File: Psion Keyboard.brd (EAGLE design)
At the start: 100 x 80 mm, 3 parts, among them X2 52745-2290

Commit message: Basic board shape.
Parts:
- moved MS1 5.08 mm to (88.9, 22.9)
- moved S2 2.84 mm to (30.5, 19.1)
- moved X2 1.80 mm to (14.0, 16.5)
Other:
- board size 100 x 80 mm -> 88.9 x 22.9 mm
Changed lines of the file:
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@@
 <setting verticaltext="up"/>
 </settings>
-<grid distance="50" unitdist="mil" unit="mil" style="lines" multiple="1" display="yes" altdistance="5" altunitdist="mil" altunit="mil"/>
+<grid distance="50" unitdist="mil" unit="mil" style="lines" multiple="1" display="yes" altdistance="0.1" altunitdist="mil" altunit="mil"/>
 <layers>
 <layer number="1" name="Top" color="4" fill="1" visible="yes" active="yes"/>
@@
 <board>
 <plain>
-<wire x1="0" y1="0" x2="100" y2="0" width="0" layer="20"/>
-<wire x1="100" y1="0" x2="100" y2="80" width="0" layer="20"/>
-<wire x1="100" y1="80" x2="0" y2="80" width="0" layer="20"/>
-<wire x1="0" y1="80" x2="0" y2="0" width="0" layer="20"/>
+<wire x1="0" y1="0" x2="88.9002" y2="0" width="0" layer="20"/>
+<wire x1="88.9002" y1="0" x2="88.900196875" y2="22.860159375" width="0" layer="20"/>
+<wire x1="88.900196875" y1="22.860159375" x2="0" y2="22.860159375" width="0" layer="20"/>
+<wire x1="0" y1="22.860159375" x2="0" y2="0" width="0" layer="20"/>
 <circle x="2.54" y="2.54" radius="1.27" width="0.000025" layer="20"/>
-<circle x="2.54" y="19.05" radius="1.27" width="0.000025" layer="20"/>
+<circle x="2.54" y="20.32" radius="1.27" width="0.000025" layer="20"/>
 </plain>
 <attributes>
@@
 </autorouter>
 <elements>
-<element name="MS1" library="adafruit" library_urn="urn:adsk.eagle:library:420" package="FEATHERWING_DIM" value="FEATHERWING_NODIM" x="93.98" y="22.86" rot="R180"/>
-<element name="S2" library="adafruit" library_urn="urn:adsk.eagle:library:420" package="EG1213" value="EG1213" x="33.02" y="20.32" rot="R180"/>
-<element name="X2" library="con-molex" library_urn="urn:adsk.eagle:library:165" package="52745-2290" value="52745-2290" x="15.24" y="17.78">
-<attribute name="MF" value="MOLEX" x="15.24" y="17.78" size="1.778" layer="27" display="off"/>
-<attribute name="MPN" value="" x="15.24" y="17.78" size="1.778" layer="27" display="off"/>
-<attribute name="OC_FARNELL" value="unknown" x="15.24" y="17.78" size="1.778" layer="27" display="off"/>
-<attribute name="OC_NEWARK" value="unknown" x="15.24" y="17.78" size="1.778" layer="27" display="off"/>
+<element name="MS1" library="adafruit" library_urn="urn:adsk.eagle:library:420" package="FEATHERWING_DIM" value="FEATHERWING_NODIM" x="88.9" y="22.86" rot="R180"/>
+<element name="S2" library="adafruit" library_urn="urn:adsk.eagle:library:420" package="EG1213" value="EG1213" x="30.48" y="19.05" rot="R180"/>
+<element name="X2" library="con-molex" library_urn="urn:adsk.eagle:library:165" package="52745-2290" value="52745-2290" x="13.97" y="16.51">
+<attribute name="MF" value="MOLEX" x="13.97" y="16.51" size="1.778" layer="27" display="off"/>
+<attribute name="MPN" value="" x="13.97" y="16.51" size="1.778" layer="27" display="off"/>
+<attribute name="OC_FARNELL" value="unknown" x="13.97" y="16.51" size="1.778" layer="27" display="off"/>
+<attribute name="OC_NEWARK" value="unknown" x="13.97" y="16.51" size="1.778" layer="27" display="off"/>
 </element>
 </elements>
@@
 <contactref element="S2" pad="1"/>
 <contactref element="MS1" pad="4"/>
-<wire x1="35.02" y1="20.32" x2="80.01" y2="21.59" width="0" layer="19" extent="1-1"/>
+<wire x1="32.48" y1="19.05" x2="74.93" y2="21.59" width="0" layer="19" extent="1-1"/>
 </signal>
 <signal name="EN">
 <contactref element="S2" pad="2"/>
 <contactref element="MS1" pad="27"/>
-<wire x1="33.02" y1="20.32" x2="74.93" y2="1.27" width="0" layer="19" extent="1-1"/>
+<wire x1="30.48" y1="19.05" x2="69.85" y2="1.27" width="0" layer="19" extent="1-1"/>
 </signal>
 <signal name="SDA">
@@
 <contactref element="X2" pad="2"/>
 <contactref element="X2" pad="5"/>
-<wire x1="11.99" y1="20.28" x2="10.49" y2="20.28" width="0" layer="19" extent="1-1"/>
-<wire x1="49.53" y1="1.27" x2="11.99" y2="20.28" width="0" layer="19" extent="1-1"/>
+<wire x1="10.72" y1="19.01" x2="9.22" y2="19.01" width="0" layer="19" extent="1-1"/>
+<wire x1="44.45" y1="1.27" x2="10.72" y2="19.01" width="0" layer="19" extent="1-1"/>
 </signal>
 <signal name="SCL">
 <contactref element="MS1" pad="18"/>
 <contactref element="X2" pad="3"/>
-<wire x1="52.07" y1="1.27" x2="10.99" y2="20.28" width="0" layer="19" extent="1-1"/>
+<wire x1="46.99" y1="1.27" x2="9.72" y2="19.01" width="0" layer="19" extent="1-1"/>
 </signal>
 <signal name="27">
 <contactref element="MS1" pad="19"/>
 <contactref element="X2" pad="4"/>
-<wire x1="54.61" y1="1.27" x2="11.49" y2="20.28" width="0" layer="19" extent="1-1"/>
+<wire x1="49.53" y1="1.27" x2="10.22" y2="19.01" width="0" layer="19" extent="1-1"/>
 </signal>
 <signal name="30">
 <contactref element="MS1" pad="20"/>
 <contactref element="X2" pad="6"/>
-<wire x1="57.15" y1="1.27" x2="12.49" y2="20.28" width="0" layer="19" extent="1-1"/>
+<wire x1="52.07" y1="1.27" x2="11.22" y2="19.01" width="0" layer="19" extent="1-1"/>
 </signal>
 <signal name="11">
 <contactref element="MS1" pad="22"/>
 <contactref element="X2" pad="7"/>
-<wire x1="12.99" y1="20.28" x2="62.23" y2="1.27" width="0" layer="19" extent="1-1"/>
+<wire x1="11.72" y1="19.01" x2="57.15" y2="1.27" width="0" layer="19" extent="1-1"/>
 </signal>
 <signal name="7">
 <contactref element="MS1" pad="23"/>
 <contactref element="X2" pad="8"/>
-<wire x1="13.49" y1="20.28" x2="64.77" y2="1.27" width="0" layer="19" extent="1-1"/>
+<wire x1="12.22" y1="19.01" x2="59.69" y2="1.27" width="0" layer="19" extent="1-1"/>
 </signal>
 <signal name="15">
 <contactref element="MS1" pad="24"/>
 <contactref element="X2" pad="9"/>
-<wire x1="13.99" y1="20.28" x2="67.31" y2="1.27" width="0" layer="19" extent="1-1"/>
+<wire x1="12.72" y1="19.01" x2="62.23" y2="1.27" width="0" layer="19" extent="1-1"/>
 </signal>
 <signal name="16">
 <contactref element="MS1" pad="25"/>
 <contactref element="X2" pad="10"/>
-<wire x1="14.49" y1="20.28" x2="69.85" y2="1.27" width="0" layer="19" extent="1-1"/>
+<wire x1="13.22" y1="19.01" x2="64.77" y2="1.27" width="0" layer="19" extent="1-1"/>
 </signal>
 <signal name="USB">
@@
 <contactref element="MS1" pad="15"/>
 <contactref element="X2" pad="21"/>
-<wire x1="19.99" y1="20.28" x2="52.07" y2="21.59" width="0" layer="19" extent="1-1"/>
+<wire x1="18.72" y1="19.01" x2="46.99" y2="21.59" width="0" layer="19" extent="1-1"/>
 </signal>
 <signal name="RXD">
 <contactref element="MS1" pad="14"/>
 <contactref element="X2" pad="20"/>
-<wire x1="19.49" y1="20.28" x2="54.61" y2="21.59" width="0" layer="19" extent="1-1"/>
+<wire x1="18.22" y1="19.01" x2="49.53" y2="21.59" width="0" layer="19" extent="1-1"/>
 </signal>
 <signal name="MISO">
 <contactref element="MS1" pad="13"/>
 <contactref element="X2" pad="19"/>
-<wire x1="18.99" y1="20.28" x2="57.15" y2="21.59" width="0" layer="19" extent="1-1"/>
+<wire x1="17.72" y1="19.01" x2="52.07" y2="21.59" width="0" layer="19" extent="1-1"/>
 </signal>
 <signal name="MOSI">
 <contactref element="MS1" pad="12"/>
 <contactref element="X2" pad="18"/>
-<wire x1="18.49" y1="20.28" x2="59.69" y2="21.59" width="0" layer="19" extent="1-1"/>
+<wire x1="17.22" y1="19.01" x2="54.61" y2="21.59" width="0" layer="19" extent="1-1"/>
 </signal>
 <signal name="SCK">
 <contactref element="MS1" pad="11"/>
 <contactref element="X2" pad="17"/>
-<wire x1="17.99" y1="20.28" x2="62.23" y2="21.59" width="0" layer="19" extent="1-1"/>
+<wire x1="16.72" y1="19.01" x2="57.15" y2="21.59" width="0" layer="19" extent="1-1"/>
 </signal>
 <signal name="A5">
 <contactref element="MS1" pad="10"/>
 <contactref element="X2" pad="16"/>
-<wire x1="17.49" y1="20.28" x2="64.77" y2="21.59" width="0" layer="19" extent="1-1"/>
+<wire x1="16.22" y1="19.01" x2="59.69" y2="21.59" width="0" layer="19" extent="1-1"/>
 </signal>
 <signal name="A4">
 <contactref element="MS1" pad="9"/>
 <contactref element="X2" pad="15"/>
-<wire x1="16.99" y1="20.28" x2="67.31" y2="21.59" width="0" layer="19" extent="1-1"/>
+<wire x1="15.72" y1="19.01" x2="62.23" y2="21.59" width="0" layer="19" extent="1-1"/>
 </signal>
 <signal name="A3">
 <contactref element="MS1" pad="8"/>
 <contactref element="X2" pad="14"/>
-<wire x1="16.49" y1="20.28" x2="69.85" y2="21.59" width="0" layer="19" extent="1-1"/>
+<wire x1="15.22" y1="19.01" x2="64.77" y2="21.59" width="0" layer="19" extent="1-1"/>
 </signal>
 <signal name="A2">
 <contactref element="MS1" pad="7"/>
 <contactref element="X2" pad="13"/>
-<wire x1="15.99" y1="20.28" x2="72.39" y2="21.59" width="0" layer="19" extent="1-1"/>
+<wire x1="14.72" y1="19.01" x2="67.31" y2="21.59" width="0" layer="19" extent="1-1"/>
 </signal>
 <signal name="A1">
 <contactref element="MS1" pad="6"/>
 <contactref element="X2" pad="12"/>
-<wire x1="15.49" y1="20.28" x2="74.93" y2="21.59" width="0" layer="19" extent="1-1"/>
+<wire x1="14.22" y1="19.01" x2="69.85" y2="21.59" width="0" layer="19" extent="1-1"/>
 </signal>
 <signal name="A0">
 <contactref element="MS1" pad="5"/>
 <contactref element="X2" pad="11"/>
-<wire x1="14.99" y1="20.28" x2="77.47" y2="21.59" width="0" layer="19" extent="1-1"/>
+<wire x1="13.72" y1="19.01" x2="72.39" y2="21.59" width="0" layer="19" extent="1-1"/>
 </signal>
 </signals>

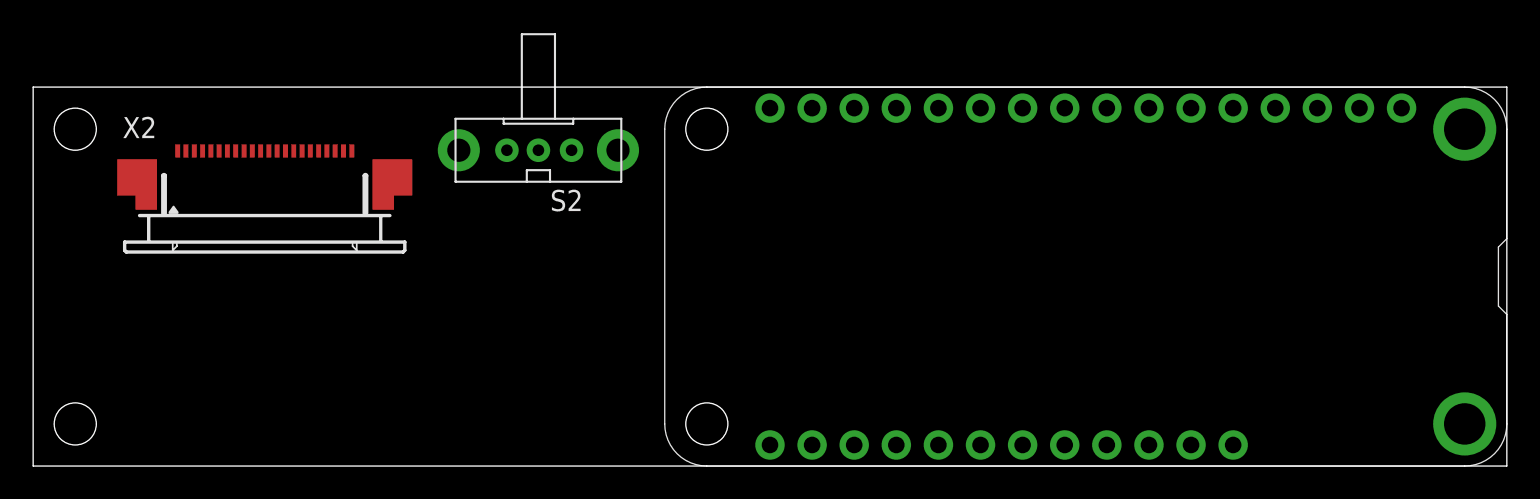
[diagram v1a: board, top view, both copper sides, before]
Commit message: Ignore .job files. General shape.
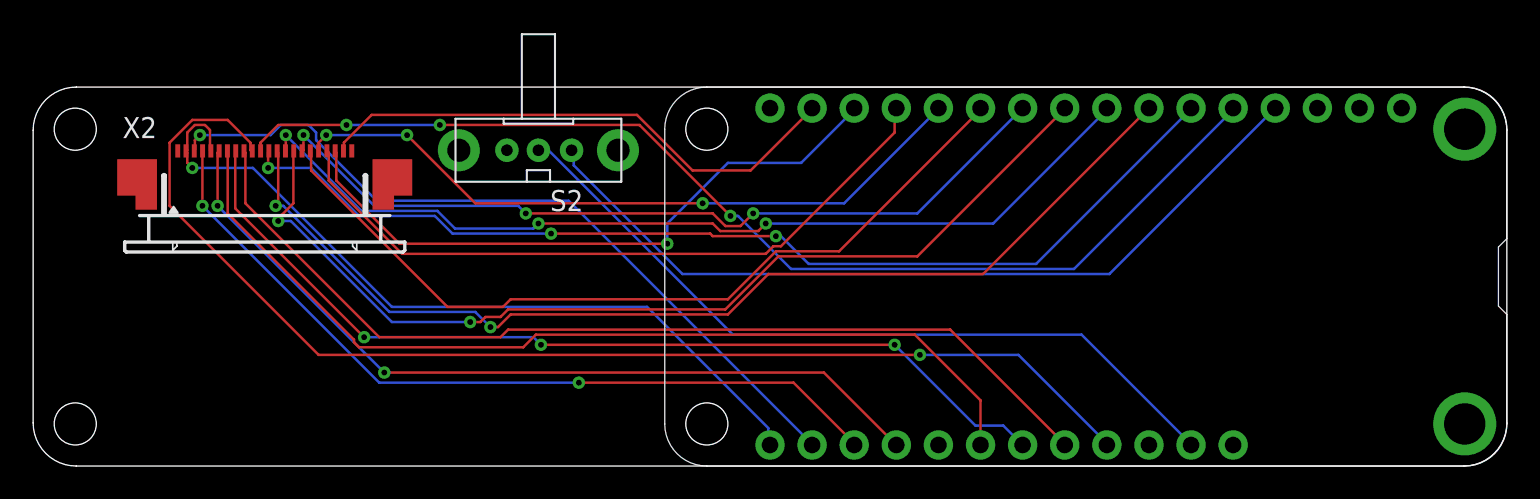
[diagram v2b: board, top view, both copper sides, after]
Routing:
- net 16: track 0.00 -> 73.0 mm, vias 0 -> 1
- net A0: track 0.00 -> 67.3 mm, vias 0 -> 3
- net A2: track 0.00 -> 64.6 mm, vias 0 -> 2
- net A1: track 0.00 -> 63.0 mm, vias 0 -> 3
- net A4: track 0.00 -> 59.9 mm, vias 0 -> 2
- net 15: track 0.00 -> 59.1 mm
- net 11: track 0.00 -> 57.3 mm
- net 7: track 0.00 -> 56.9 mm, vias 0 -> 3
- net A3: track 0.00 -> 56.3 mm, vias 0 -> 3
- net 30: track 0.00 -> 50.3 mm, vias 0 -> 2
- net GND: track 0.00 -> 50.2 mm
- net SCK: track 0.00 -> 50.0 mm
- net A5: track 0.00 -> 49.6 mm, vias 0 -> 3
- net 27: track 0.00 -> 48.7 mm, vias 0 -> 2
- net SDA: track 0.00 -> 47.6 mm, vias 0 -> 1
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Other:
- outline, holes or cut-outs redrawn
